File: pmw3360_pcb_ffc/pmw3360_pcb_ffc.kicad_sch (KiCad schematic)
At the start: 20 parts, among them J1 Interface, U1 PMW3360DM-T2QU, U2 TPS73601DBV

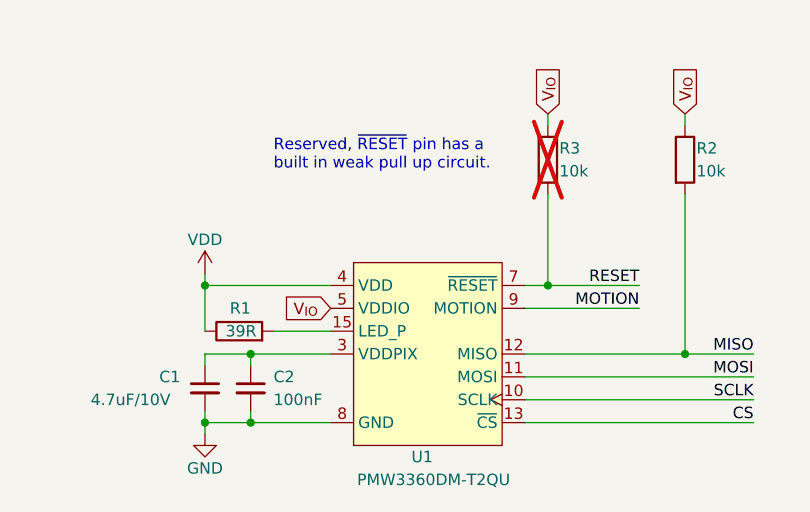
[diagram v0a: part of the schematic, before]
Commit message: Update symbol references
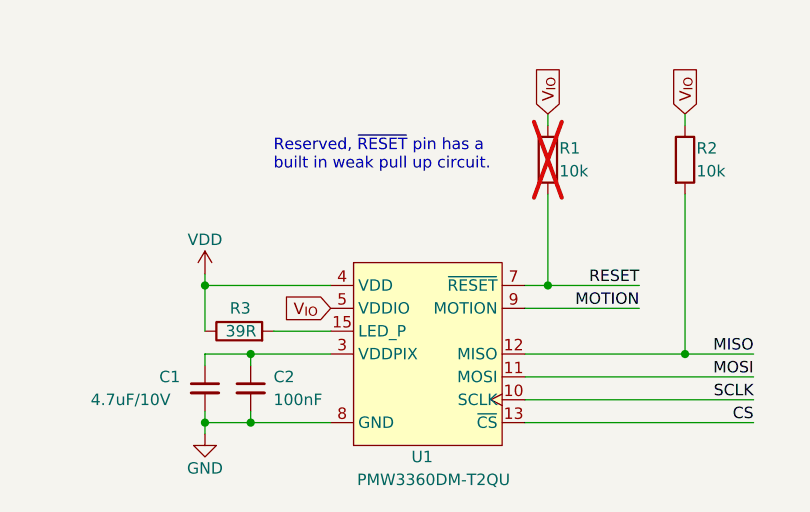
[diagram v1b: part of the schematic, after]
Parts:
- renumbered R3 to R1, R1 to R3
